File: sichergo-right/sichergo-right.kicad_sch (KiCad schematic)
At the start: 27 parts, among them J1 Conn_01x04_Pin, Q1 2N7002, SW1 MS-22C01-G010, U1 YTS1C0033BBG01, U2 STM32F103C8Tx, U3 SN74LVC1G125DBV, U4 SN74LVC1G125DBV, Y1 Crystal_GND24

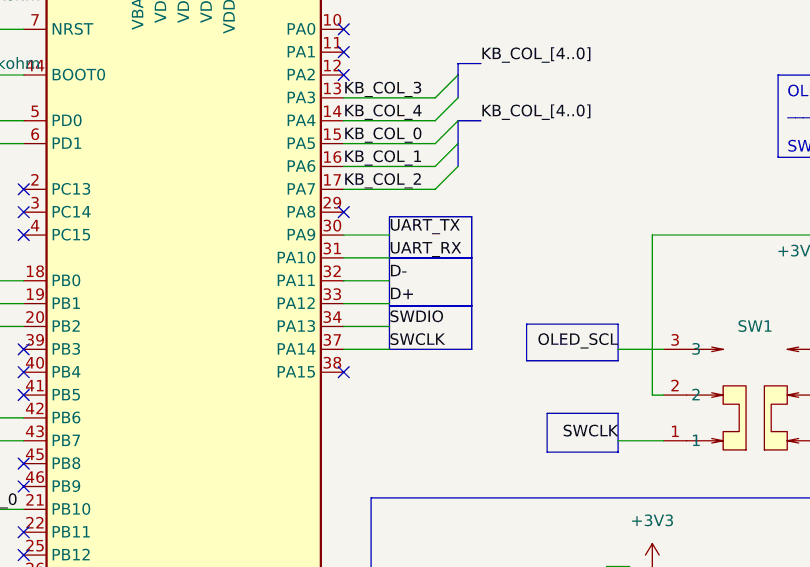
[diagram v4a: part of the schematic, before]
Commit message: Finish routing right side
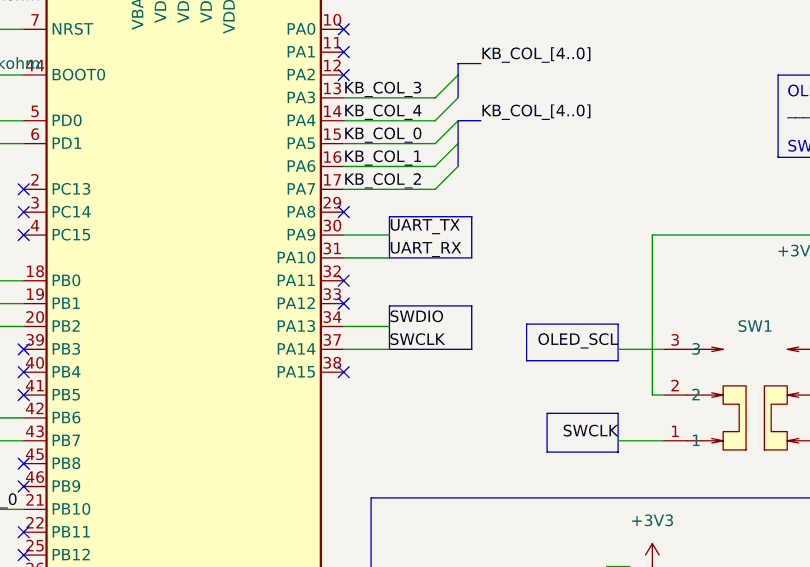
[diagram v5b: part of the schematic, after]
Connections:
- net D+: no longer names the net of U2.33 (PA12)
- net D-: no longer names the net of U2.32 (PA11)
- no-connect marks 17 -> 19
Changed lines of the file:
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@@
+	)
+	(no_connect
+		(at 205.74 83.82)
 	)
 	(no_connect
@@
 	(no_connect
 		(at 170.18 78.74)
+	)
+	(no_connect
+		(at 205.74 86.36)
 	)
 	(no_connect
@@
 	(wire
 		(pts
-			(xy 205.74 83.82) (xy 210.82 83.82)
-		)
-		(stroke
-			(width 0)
-			(type default)
-		)
-	)
-	(wire
-		(pts
 			(xy 254 123.19) (xy 265.43 123.19)
 		)
@@
 		(pts
 			(xy 152.4 81.28) (xy 154.94 81.28)
-		)
-		(stroke
-			(width 0)
-			(type default)
-		)
-	)
-	(wire
-		(pts
-			(xy 205.74 86.36) (xy 210.82 86.36)
 		)
 		(stroke
@@
 			(type default)
 			(color 194 0 194 1)
-		)
-		(fill
-			(type none)
-		)
-	)
-	(rectangle
-		(start 210.82 81.28)
-		(end 219.964 86.614)
-		(stroke
-			(width 0)
-			(type default)
-			(color 132 0 0 1)
 		)
 		(fill
@@
 		)
 	)
-	(label "D+"
-		(at 210.82 86.36 0)
-		(effects
-			(font
-				(size 1.27 1.27)
-			)
-			(justify left bottom)
-		)
-	)
 	(label "SWCLK"
 		(at 236.22 101.6 180)
@@
 		(effects
 			(font
-				(size 1.27 1.27)
-			)
-			(justify left bottom)
-		)
-	)
-	(label "D-"
-		(at 210.82 83.82 0)
-		(effects
-			(font

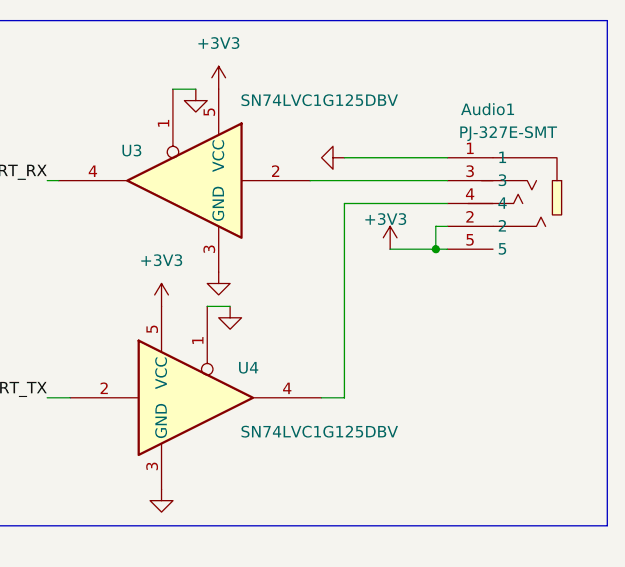
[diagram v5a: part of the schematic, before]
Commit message: fix left side USB C
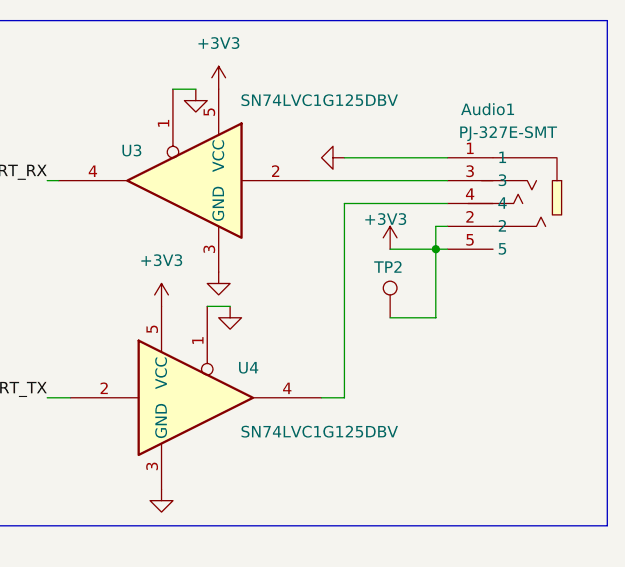
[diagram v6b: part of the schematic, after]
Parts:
- added TP2: TestPoint, TestPoint:TestPoint_THTPad_1.0x1.0mm_Drill0.5mm, symbol Connector:TestPoint
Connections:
- net +3V3: now also TP2.1
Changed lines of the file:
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@@
 	(wire
 		(pts
+			(xy 259.08 140.97) (xy 264.16 140.97)
+		)
+		(stroke
+			(width 0)
+			(type default)
+		)
+	)
+	(wire
+		(pts
 			(xy 213.36 33.02) (xy 222.25 33.02)
 		)
@@
 	(wire
 		(pts
+			(xy 264.16 140.97) (xy 264.16 133.35)
+		)
+		(stroke
+			(width 0)
+			(type default)
+		)
+	)
+	(wire
+		(pts
 			(xy 113.03 132.08) (xy 113.03 139.7)
 		)
@@
 					(unit 1)
 				)
+			)
+		)
+	)
+	(symbol
+		(lib_id "Connector:TestPoint")
+		(at 259.08 140.97 0)
+		(unit 1)
+		(exclude_from_sim no)
+		(in_bom yes)
+		(on_board yes)
+		(dnp no)
+		(property "Reference" "TP2"
+			(at 257.302 135.382 0)
+			(effects
+				(font
+					(size 1.27 1.27)
+				)
+				(justify left)
+			)
+		)
+		(property "Value" "TestPoint"
+			(at 261.62 138.9379 0)
+			(effects
+				(font
+					(size 1.27 1.27)
+				)
+				(justify left)
+				(hide yes)
+			)
+		)
+		(property "Footprint" "TestPoint:TestPoint_THTPad_1.0x1.0mm_Drill0.5mm"
+			(at 264.16 140.97 0)
+			(effects
+				(font
+					(size 1.27 1.27)
+				)
+				(hide yes)
+			)
+		)
+		(property "Datasheet" "~"
+			(at 264.16 140.97 0)
+			(effects
+				(font
+					(size 1.27 1.27)
+				)
+				(hide yes)
+			)
+		)
+		(property "Description" "test point"
+			(at 259.08 140.97 0)
+			(effects
+				(font
+					(size 1.27 1.27)
+				)
+				(hide yes)
+			)
+		)
+		(pin "1"
+		)
+		(instances
+			(project "sichergo-right"
+				(path "/7d6715fb-1e77-4b7f-bc05-ec156d7f2ccd"
+					(reference "TP2")
+					(unit 1)
+				)
